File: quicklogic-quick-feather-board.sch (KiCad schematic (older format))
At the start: 54 parts, among them IC1 EOS-S3, J5 0473460001, Q1 BSS138AKA, Q2 BSS84, U1 TPS62821DLCR, U2 MCP73831T-2ACI_OT, U3 GD25Q16CWIGR, U4 DPS310, U5 MC3635, X1 ECS-_327-12_5-34B-TR

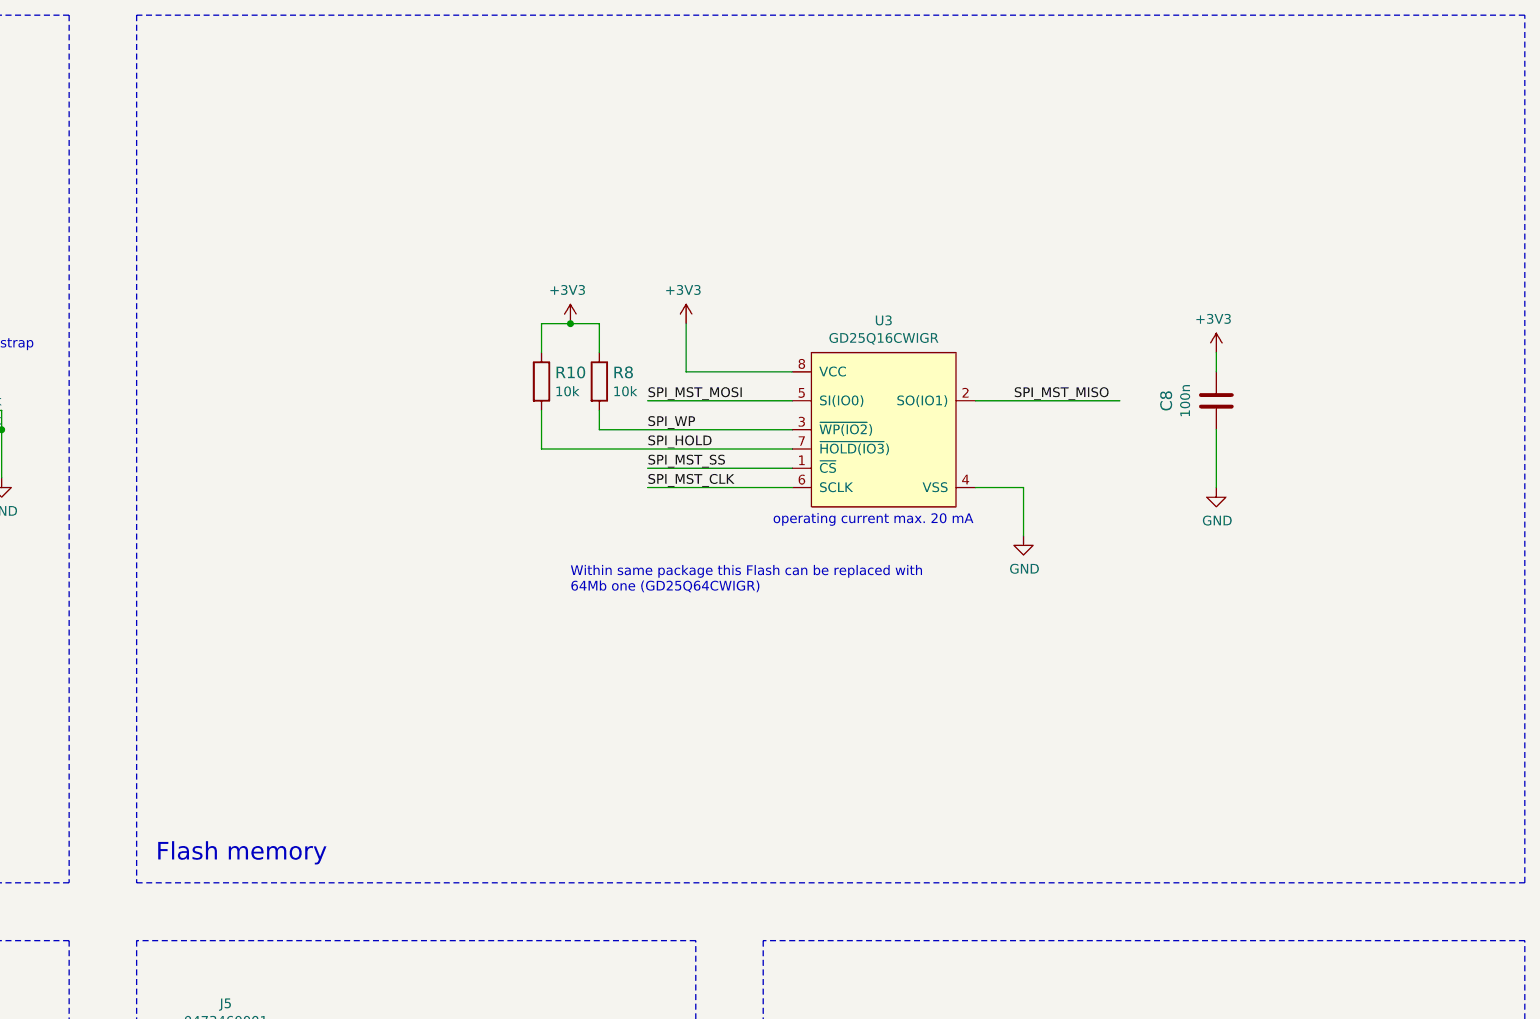
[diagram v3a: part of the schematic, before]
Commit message: Added BTN/LED section
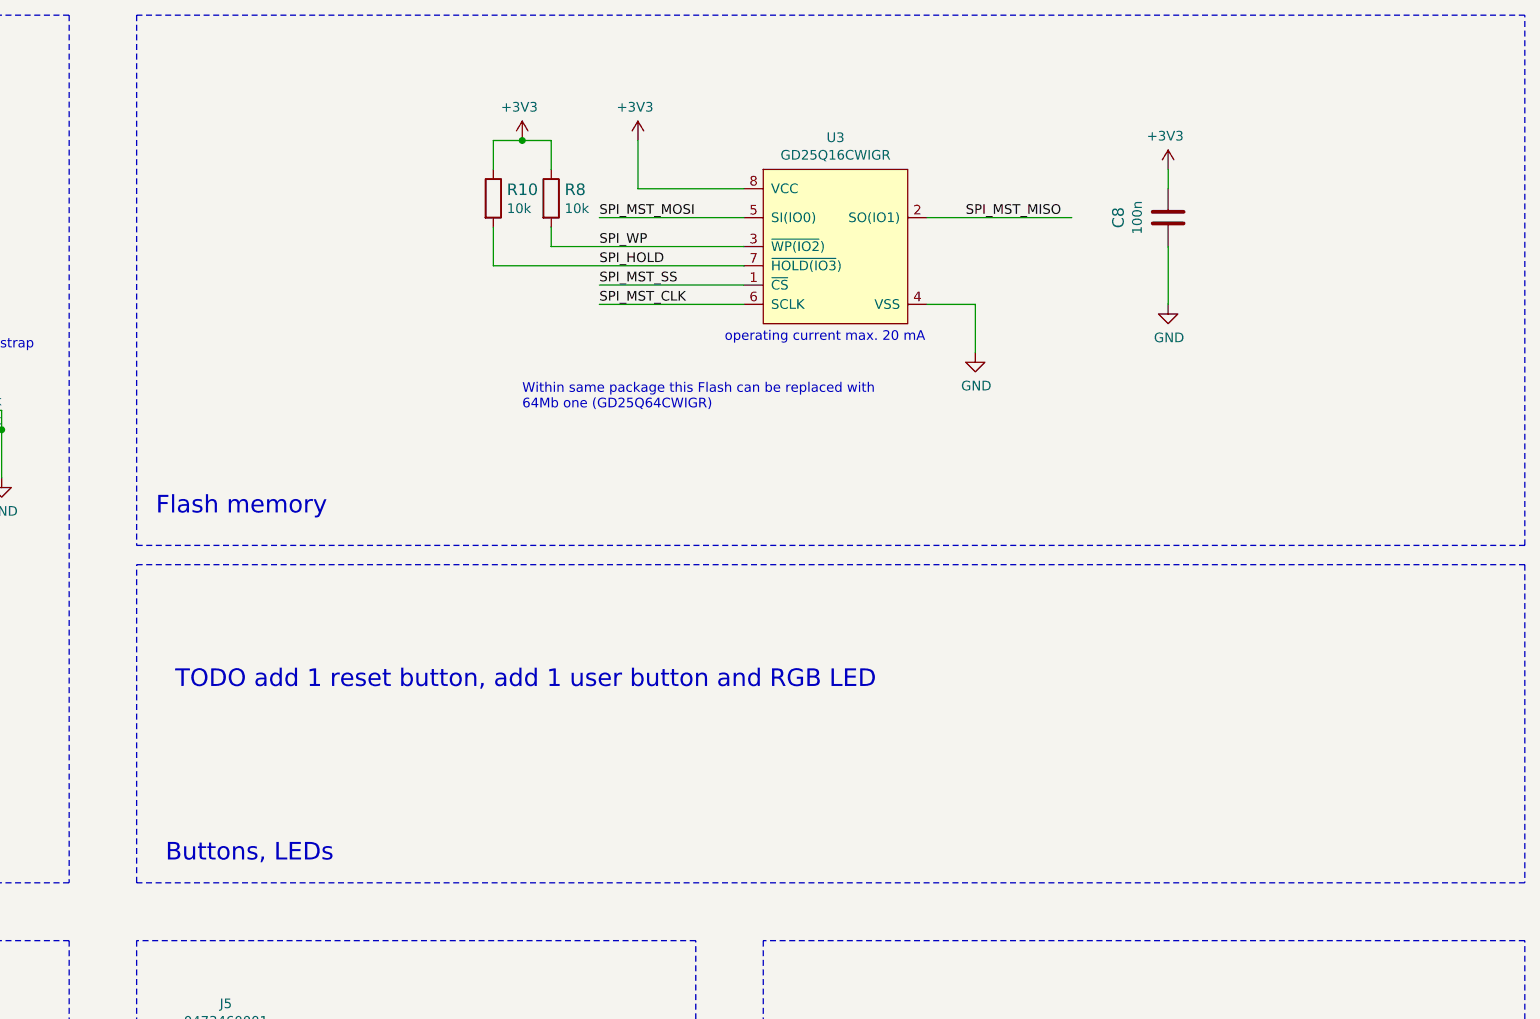
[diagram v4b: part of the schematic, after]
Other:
- note added: "Buttons, LEDs"
- note added: "TODO add 1 reset button, add 1 user button and RGB LED"
- moved on the sheet: C8, R10, R8, U3
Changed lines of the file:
@@
 L quicklogic-quick-feather-board:R_10k_0402 R8
 U 1 1 5DC453B0
-P 11000 2600
-F 0 "R8" V 10955 2670 60  0000 L CNN
-F 1 "R_10k_0402" H 11000 2450 60  0001 C CNN
-F 2 "quicklogic-quick-feather-board-footprints:0402-res" H 11200 2800 60  0001 L CNN
-F 3 "" H 11000 2600 50  0001 C CNN
-F 4 "VISHAY" H 11200 3000 60  0001 L CNN "Manufacturer"
-F 5 "CRCW040210K0FKEDHP" H 11200 2900 60  0001 L CNN "MPN"
-F 6 "10k" V 11053 2670 50  0000 L CNN "Val"
-	1    11000 2600
+P 10750 1650
+F 0 "R8" V 10705 1720 60  0000 L CNN
+F 1 "R_10k_0402" H 10750 1500 60  0001 C CNN
+F 2 "quicklogic-quick-feather-board-footprints:0402-res" H 10950 1850 60  0001 L CNN
+F 3 "" H 10750 1650 50  0001 C CNN
+F 4 "VISHAY" H 10950 2050 60  0001 L CNN "Manufacturer"
+F 5 "CRCW040210K0FKEDHP" H 10950 1950 60  0001 L CNN "MPN"
+F 6 "10k" V 10803 1720 50  0000 L CNN "Val"
+	1    10750 1650
 	0    1    1    0
 $EndComp
@@
 L quicklogic-quick-feather-board:R_10k_0402 R10
 U 1 1 5DC484F8
-P 10700 2600
-F 0 "R10" V 10655 2670 60  0000 L CNN
-F 1 "R_10k_0402" H 10700 2450 60  0001 C CNN
-F 2 "quicklogic-quick-feather-board-footprints:0402-res" H 10900 2800 60  0001 L CNN
-F 3 "" H 10700 2600 50  0001 C CNN
-F 4 "VISHAY" H 10900 3000 60  0001 L CNN "Manufacturer"
-F 5 "CRCW040210K0FKEDHP" H 10900 2900 60  0001 L CNN "MPN"
-F 6 "10k" V 10753 2670 50  0000 L CNN "Val"
-	1    10700 2600
+P 10450 1650
+F 0 "R10" V 10405 1720 60  0000 L CNN
+F 1 "R_10k_0402" H 10450 1500 60  0001 C CNN
+F 2 "quicklogic-quick-feather-board-footprints:0402-res" H 10650 1850 60  0001 L CNN
+F 3 "" H 10450 1650 50  0001 C CNN
+F 4 "VISHAY" H 10650 2050 60  0001 L CNN "Manufacturer"
+F 5 "CRCW040210K0FKEDHP" H 10650 1950 60  0001 L CNN "MPN"
+F 6 "10k" V 10503 1720 50  0000 L CNN "Val"
+	1    10450 1650
 	0    1    1    0
 $EndComp
 Wire Wire Line
-	12950 2700 13700 2700
-Wire Wire Line
-	11250 2700 12000 2700
-Wire Wire Line
-	11250 3150 12000 3150
-Wire Wire Line
-	11250 3050 12000 3050
-Text Notes 10850 3700 0    50   ~ 0
+	12700 1750 13450 1750
+Wire Wire Line
+	11000 1750 11750 1750
+Wire Wire Line
+	11000 2200 11750 2200
+Wire Wire Line
+	11000 2100 11750 2100
+Text Notes 10600 2750 0    50   ~ 0
 Within same package this Flash can be replaced with \n64Mb one (GD25Q64CWIGR)
 Wire Wire Line
@@
 $EndBitmap
 Wire Wire Line
-	12000 2550 11450 2550
+	11750 1600 11200 1600
 $Comp
 L quicklogic-quick-feather-board:C_100n_0402_6V3 C8
 U 1 1 5DDB4C4D
-P 14200 2700
-F 0 "C8" V 13942 2700 60  0000 C CNN
-F 1 "C_100n_0402_6V3" H 14200 2550 60  0001 C CNN
-F 2 "quicklogic-quick-feather-board-footprints:0402-cap" H 14400 2900 60  0001 L CNN
-F 3 "" H 14200 2700 50  0001 C CNN
-F 4 "Walsin" H 14400 3100 60  0001 L CNN "Manufacturer"
-F 5 "0402X104K6R3CT" H 14400 3000 60  0001 L CNN "MPN"
-F 6 "100n" V 14040 2700 50  0000 C CNN "Val"
-	1    14200 2700
+P 13950 1750
+F 0 "C8" V 13692 1750 60  0000 C CNN
+F 1 "C_100n_0402_6V3" H 13950 1600 60  0001 C CNN
+F 2 "quicklogic-quick-feather-board-footprints:0402-cap" H 14150 1950 60  0001 L CNN
+F 3 "" H 13950 1750 50  0001 C CNN
+F 4 "Walsin" H 14150 2150 60  0001 L CNN "Manufacturer"
+F 5 "0402X104K6R3CT" H 14150 2050 60  0001 L CNN "MPN"
+F 6 "100n" V 13790 1750 50  0000 C CNN "Val"
+	1    13950 1750
 	1    0    0    -1
 $EndComp
@@
 L quicklogic-quick-feather-board:GND #PWR0111
 U 1 1 5DDBDD77
-P 13200 3400
-F 0 "#PWR0111" H 13200 3150 50  0001 C CNN
-F 1 "GND" H 13205 3227 50  0000 C CNN
-F 2 "" H 13200 3400 50  0001 C CNN
-F 3 "" H 13200 3400 50  0001 C CNN
-	1    13200 3400
-	1    0    0    -1
-$EndComp
-Text Label 11250 2850 0    50   ~ 0
+P 12950 2450
+F 0 "#PWR0111" H 12950 2200 50  0001 C CNN
+F 1 "GND" H 12955 2277 50  0000 C CNN
+F 2 "" H 12950 2450 50  0001 C CNN
+F 3 "" H 12950 2450 50  0001 C CNN
+	1    12950 2450
+	1    0    0    -1
+$EndComp
+Text Label 11000 1900 0    50   ~ 0
 SPI_WP
-Text Label 11250 2950 0    50   ~ 0
+Text Label 11000 2000 0    50   ~ 0
 SPI_HOLD
-Text Label 13150 2700 0    50   ~ 0
+Text Label 12900 1750 0    50   ~ 0
 SPI_MST_MISO
-Text Label 11250 2700 0    50   ~ 0
+Text Label 11000 1750 0    50   ~ 0
 SPI_MST_MOSI
-Text Label 11250 3050 0    50   ~ 0
+Text Label 11000 2100 0    50   ~ 0
 SPI_MST_SS
-Text Label 11250 3150 0    50   ~ 0
+Text Label 11000 2200 0    50   ~ 0
 SPI_MST_CLK
 $Comp
 L quicklogic-quick-feather-board:GD25Q16CWIGR U3
 U 1 1 5DDDF93D
-P 12100 2450
-F 0 "U3" H 12475 2615 50  0000 C CNN
-F 1 "GD25Q16CWIGR" H 12475 2524 50  0000 C CNN
-F 2 "quicklogic-quick-feather-board-footprints:GD25Q16CWIG" H 12050 2400 50  0001 C CNN
-F 3 "http://www.gigadevice.com/datasheet/gd25q16c/" H 12150 2500 50  0001 C CNN
-	1    12100 2450
+P 11850 1500
+F 0 "U3" H 12225 1665 50  0000 C CNN
+F 1 "GD25Q16CWIGR" H 12225 1574 50  0000 C CNN
+F 2 "quicklogic-quick-feather-board-footprints:GD25Q16CWIG" H 11800 1450 50  0001 C CNN
+F 3 "http://www.gigadevice.com/datasheet/gd25q16c/" H 11900 1550 50  0001 C CNN
+	1    11850 1500
 	1    0    0    -1
 $EndComp
@@
 	8250 700  8250 5200
 Wire Notes Line
-	8600 700  8600 5200
-Wire Notes Line
-	8600 5200 15800 5200
-Wire Notes Line
-	15800 5200 15800 700
+	8600 700  8600 3450
+Wire Notes Line
+	8600 3450 15800 3450
+Wire Notes Line
+	15800 3450 15800 700
 Wire Notes Line
 	15800 700  8600 700
@@
 Text Notes 800  10100 0    91   ~ 0
 Supply
-Text Notes 8700 5100 0    91   ~ 0
+Text Notes 8700 3300 0    91   ~ 0
 Flash memory
 Text Notes 8700 7700 0    91   ~ 0
@@
 L quicklogic-quick-feather-board:+3V3 #PWR0113
 U 1 1 5DE33E97
-P 11450 2250
-F 0 "#PWR0113" H 11450 2250 50  0001 C CNN
-F 1 "+3V3" H 11435 2373 50  0000 C CNN
-F 2 "" H 11450 2250 50  0001 C CNN
-F 3 "" H 11450 2250 50  0001 C CNN
-	1    11450 2250
+P 11200 1300
+F 0 "#PWR0113" H 11200 1300 50  0001 C CNN
+F 1 "+3V3" H 11185 1423 50  0000 C CNN
+F 2 "" H 11200 1300 50  0001 C CNN
+F 3 "" H 11200 1300 50  0001 C CNN
+	1    11200 1300
 	1    0    0    -1
 $EndComp
@@
 L quicklogic-quick-feather-board:+3V3 #PWR0114
 U 1 1 5DE34948
-P 14200 2400
-F 0 "#PWR0114" H 14200 2400 50  0001 C CNN
-F 1 "+3V3" H 14185 2523 50  0000 C CNN
-F 2 "" H 14200 2400 50  0001 C CNN
-F 3 "" H 14200 2400 50  0001 C CNN
-	1    14200 2400
-	1    0    0    -1
-$EndComp
-Wire Wire Line
-	12950 3150 13200 3150
-Wire Wire Line
-	13200 3150 13200 3400
-Wire Wire Line
-	14200 2850 14200 3150
+P 13950 1450
+F 0 "#PWR0114" H 13950 1450 50  0001 C CNN
+F 1 "+3V3" H 13935 1573 50  0000 C CNN
+F 2 "" H 13950 1450 50  0001 C CNN
+F 3 "" H 13950 1450 50  0001 C CNN
+	1    13950 1450
+	1    0    0    -1
+$EndComp
+Wire Wire Line
+	12700 2200 12950 2200
+Wire Wire Line
+	12950 2200 12950 2450
+Wire Wire Line
+	13950 1900 13950 2200
 $Comp
 L quicklogic-quick-feather-board:GND #PWR0115
 U 1 1 5DE3FA98
-P 14200 3150
-F 0 "#PWR0115" H 14200 2900 50  0001 C CNN
-F 1 "GND" H 14205 2977 50  0000 C CNN
-F 2 "" H 14200 3150 50  0001 C CNN
-F 3 "" H 14200 3150 50  0001 C CNN
-	1    14200 3150
-	1    0    0    -1
-$EndComp
-Wire Wire Line
-	14200 2450 14200 2550
+P 13950 2200
+F 0 "#PWR0115" H 13950 1950 50  0001 C CNN
+F 1 "GND" H 13955 2027 50  0000 C CNN
+F 2 "" H 13950 2200 50  0001 C CNN
+F 3 "" H 13950 2200 50  0001 C CNN
+	1    13950 2200
+	1    0    0    -1
+$EndComp
+Wire Wire Line
+	13950 1500 13950 1600
 $Comp
 L quicklogic-quick-feather-board:+3V3 #PWR0116
@@
 L quicklogic-quick-feather-board:+3V3 #PWR0110
 U 1 1 5DE86C59
-P 10850 2250
-F 0 "#PWR0110" H 10850 2250 50  0001 C CNN
-F 1 "+3V3" H 10835 2373 50  0000 C CNN
-F 2 "" H 10850 2250 50  0001 C CNN
-F 3 "" H 10850 2250 50  0001 C CNN
-	1    10850 2250
-	1    0    0    -1
-$EndComp
-Wire Wire Line
-	11000 2450 11000 2300
-Wire Wire Line
-	11000 2300 10850 2300
-Wire Wire Line
-	10700 2450 10700 2300
-Wire Wire Line
-	10700 2300 10850 2300
-Connection ~ 10850 2300
-Wire Wire Line
-	11000 2850 11000 2750
-Wire Wire Line
-	11000 2850 12000 2850
-Wire Wire Line
-	10700 2950 10700 2750
-Wire Wire Line
-	10700 2950 12000 2950
-Wire Wire Line
-	11450 2300 11450 2550
+P 10600 1300
+F 0 "#PWR0110" H 10600 1300 50  0001 C CNN
+F 1 "+3V3" H 10585 1423 50  0000 C CNN
+F 2 "" H 10600 1300 50  0001 C CNN
+F 3 "" H 10600 1300 50  0001 C CNN
+	1    10600 1300
+	1    0    0    -1
+$EndComp
+Wire Wire Line
+	10750 1500 10750 1350
+Wire Wire Line
+	10750 1350 10600 1350
+Wire Wire Line
+	10450 1500 10450 1350
+Wire Wire Line
+	10450 1350 10600 1350
+Connection ~ 10600 1350
+Wire Wire Line
+	10750 1900 10750 1800
+Wire Wire Line
+	10750 1900 11750 1900
+Wire Wire Line
+	10450 2000 10450 1800
+Wire Wire Line
+	10450 2000 11750 2000
+Wire Wire Line
+	11200 1350 11200 1600
 $Comp
 L quicklogic-quick-feather-board:DPS310 U4
@@
 Text Notes 3300 5000 0    50   ~ 0
 The multi-functional IOs have four programmable drive \nstrength states: 2 mA, 4 mA, 8 mA, 12 mA \n(refer to datasheet page 92)
-Text Notes 11900 3350 0    50   ~ 0
+Text Notes 11650 2400 0    50   ~ 0
 operating current max. 20 mA
 Text Notes 12350 9550 0    50   ~ 0
 operating current  for 1V8 supply\nmax. 36mA\nlow-power mode: max. 2.8mA
+Wire Notes Line
+	8600 3550 15800 3550
+Wire Notes Line
+	15800 3550 15800 5200
+Wire Notes Line
+	15800 5200 8600 5200
+Wire Notes Line
+	8600 5200 8600 3550
+Text Notes 8750 5100 0    91   ~ 0
+Buttons, LEDs
+Text Notes 8800 4200 0    91   ~ 0
+TODO add 1 reset button, add 1 user button and RGB LED
 $EndSCHEMATC

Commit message: Design updated after internal review
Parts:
- removed R18, R20: R_10k_0402, quicklogic-quick-feather-board-footprints:0402-res, symbol quicklogic-quick-feather-board:R_10k_0402
- added C14, C16: C_4u7_0603, quicklogic-quick-feather-board-footprints:0603-cap, symbol quicklogic-quick-feather-board:C_4u7_0603
- added D11, D5: TPD2EUSB30DRTR, quicklogic-quick-feather-board-footprints:SOT-3, symbol quicklogic-quick-feather-board:TPD2EUSB30DRTR
- added D4: UHD1110-FKA, quicklogic-quick-feather-board-footprints:LED-RGB-5DS-UHD1110-FKA, symbol quicklogic-quick-feather-board:UHD1110-FKA
- added J1: SHF-105-01-L-D-SM, quicklogic-quick-feather-board-footprints:SHF-105-01-L-D-SM, symbol quicklogic-quick-feather-board:SHF-105-01-L-D-SM
- added J2: 1x12_pinhead, quicklogic-quick-feather-board-footprints:1x12_pinhead, symbol quicklogic-quick-feather-board:1x12_pinhead
- added J3: 1x16_pinhead, quicklogic-quick-feather-board-footprints:1x16_pinhead, symbol quicklogic-quick-feather-board:1x16_pinhead
- added R18, R20: R_4k7_0402, quicklogic-quick-feather-board-footprints:0402-res, symbol quicklogic-quick-feather-board:R_4k7_0402
- added R23: R_10k_0402, quicklogic-quick-feather-board-footprints:0402-res, symbol quicklogic-quick-feather-board:R_10k_0402
- added S1, S2: TL3365AF180QG, quicklogic-quick-feather-board-footprints:SW_SPST_4.2x3.2, symbol quicklogic-quick-feather-board:TL3365AF180QG
- added TP3, TP4, TP5, TP6, TP7: TP_SMD1MM, quicklogic-quick-feather-board-footprints:Testpoint_smd_1mm, symbol quicklogic-quick-feather-board:TP_SMD1MM
- gave numbers to parts that had none: 4
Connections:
- net labels added: HEADER_3V3, HEADER_A0, HEADER_A1, HEADER_A2, HEADER_A3, HEADER_A4, HEADER_A5, HEADER_AREF, HEADER_BAT, HEADER_En, HEADER_GND, HEADER_MISO, HEADER_MOSI, HEADER_P10, HEADER_P11, HEADER_P5, HEADER_P6, HEADER_P7, HEADER_P8, HEADER_P9, HEADER_RX, HEADER_SCK, HEADER_TX, HEADER_USB, LED_B, LED_G, LED_R, SWD_SO, SYS_RST, USR_BUTTON, VDD1, VDD2
- net labels removed: IO24, IO25, IO30, RST_N, SPI_SLV_CLK, SPI_SLV_MISO, SPI_SLV_MOSI, SPI_SLV_SS
- wire segments 214 -> 279
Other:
- note added: "Mount R23 for debug mode, \notherwise R22"
- note added: "SWD, Feather header"
- note removed: "TODO add 1 reset button, add 1 user button and RGB LED"
- note removed: "TODO: add RST source"
- moved on the sheet: C8, R10, R21, R22, R8, TP1, TP2, U3

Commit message: Changes to header, tweaks to LED, added BAT connector
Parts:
- removed TP3: TP_SMD1MM, quicklogic-quick-feather-board-footprints:Testpoint_smd_1mm, symbol quicklogic-quick-feather-board:TP_SMD1MM
- added J?: S2B-PH-SM4-TB_LF__SN_, antmicro-footprints:PinHeader_2x1mm_P2mm_SMD_RA, symbol antmicroRectangularConnectorsHeadersMalePins:S2B-PH-SM4-TB_LF__SN_
- added Q? (x3): BSS138AKA, quicklogic-quick-feather-board-footprints:SOT-23-3, symbol quicklogic-quick-feather-board:BSS138AKA
- added R? (x3): R_100R_0402, quicklogic-quick-feather-board-footprints:0402-res, symbol quicklogic-quick-feather-board:R_100R_0402
- added R?: EXB2HV220JV, quicklogic-quick-feather-board-footprints:R_Array_Convex_8x0602, symbol quicklogic-quick-feather-board:EXB2HV220JV
- added R? (x3): R_22R_0402, quicklogic-quick-feather-board-footprints:0402-res, symbol quicklogic-quick-feather-board:R_22R_0402
- added TP?: TP_SMD1MM, quicklogic-quick-feather-board-footprints:Testpoint_smd_1mm, symbol quicklogic-quick-feather-board:TP_SMD1MM
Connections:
- net labels added: Q_LED_B, Q_LED_G, Q_LED_R
- net labels removed: HEADER_A0, HEADER_A1, HEADER_A2, HEADER_A3, HEADER_A4, HEADER_AREF, HEADER_En, HEADER_GND, HEADER_P10, HEADER_P11, HEADER_P5, HEADER_P7, HEADER_P8, HEADER_P9, HEADER_USB
- wire segments 279 -> 281
- no-connect marks 0 -> 20
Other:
- moved on the sheet: C1, C10, C11, C3, C4, D1, D4, J2, J3, L1, R1, R18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
